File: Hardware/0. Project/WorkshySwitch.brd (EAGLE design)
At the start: 35 x 45 mm, 52 parts, among them J1 ICSP, K1 G3MB-202P, U2 HLK-PM01

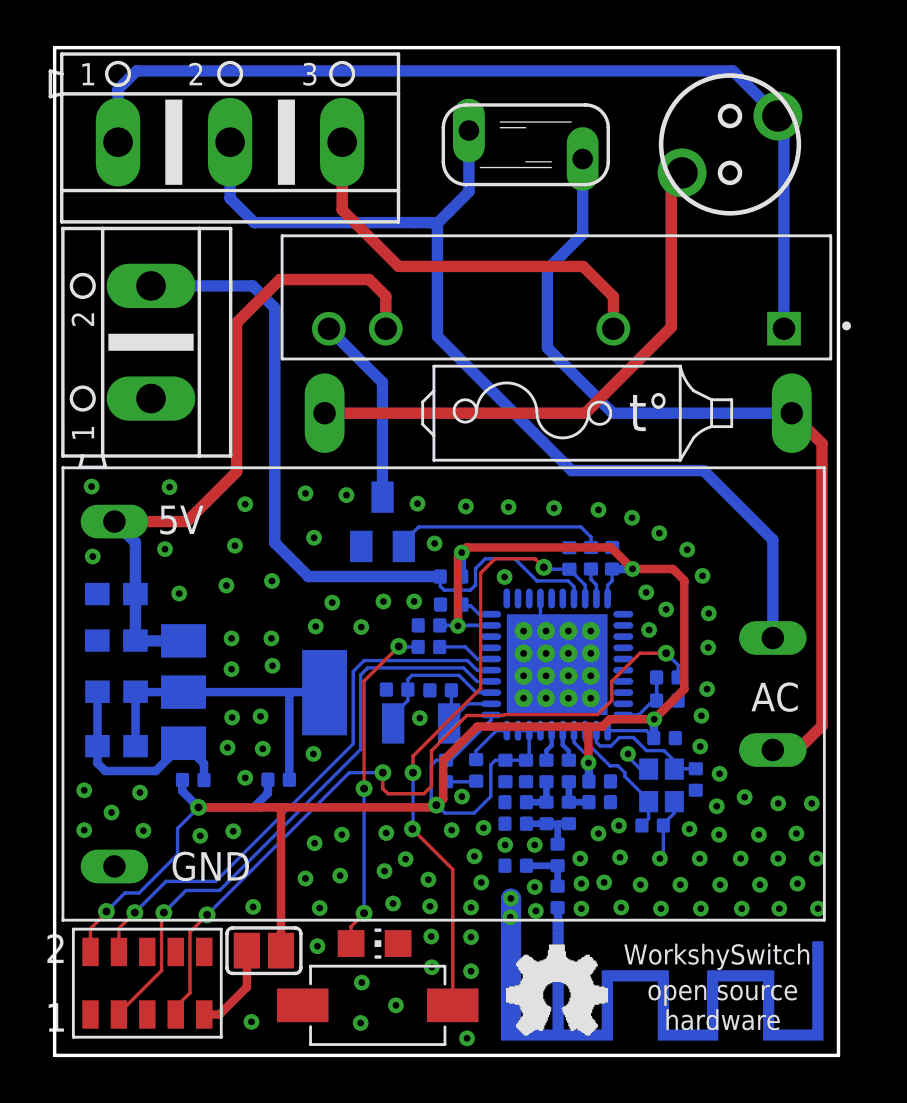
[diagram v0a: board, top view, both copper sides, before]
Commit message: 3D PCB Model Generated
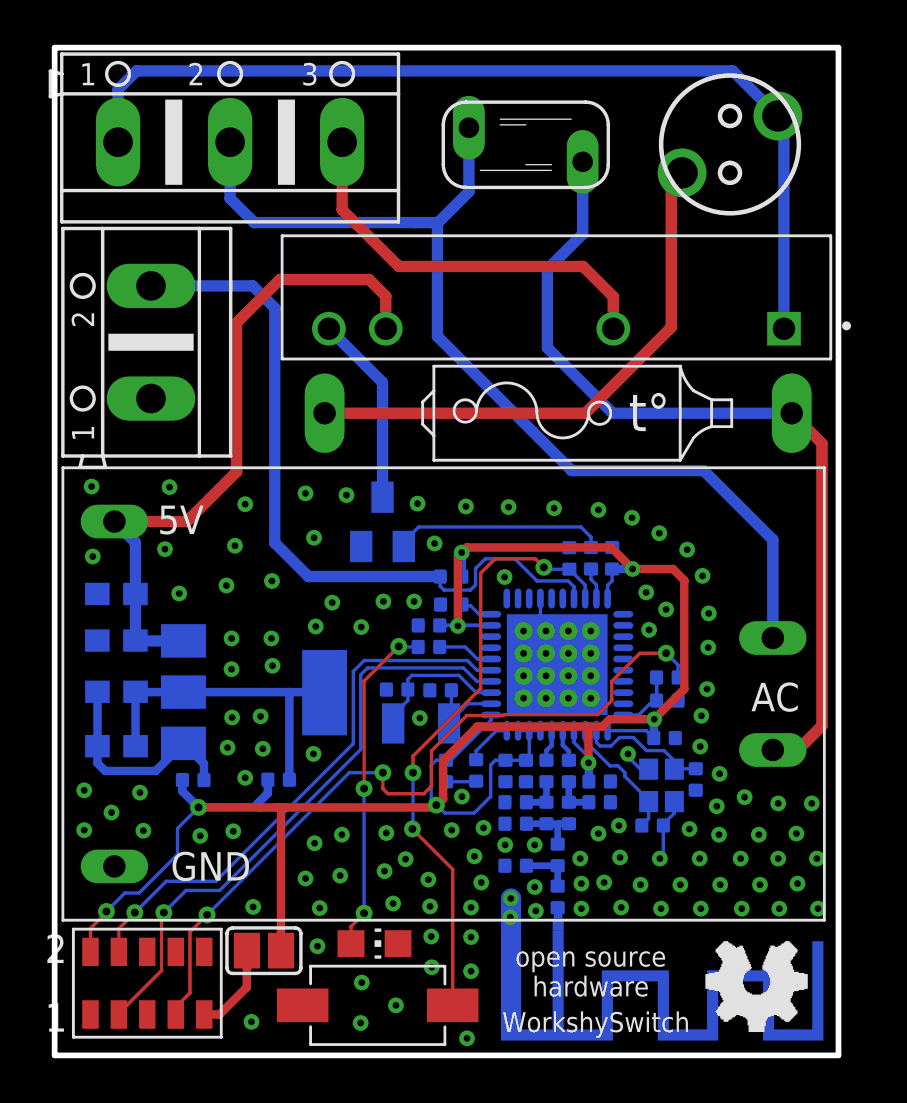
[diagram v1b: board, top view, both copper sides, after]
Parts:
- C22: value (none) -> C0402
- R5: device varistor:S05K11 -> varistor:S05K17

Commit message: Components values added
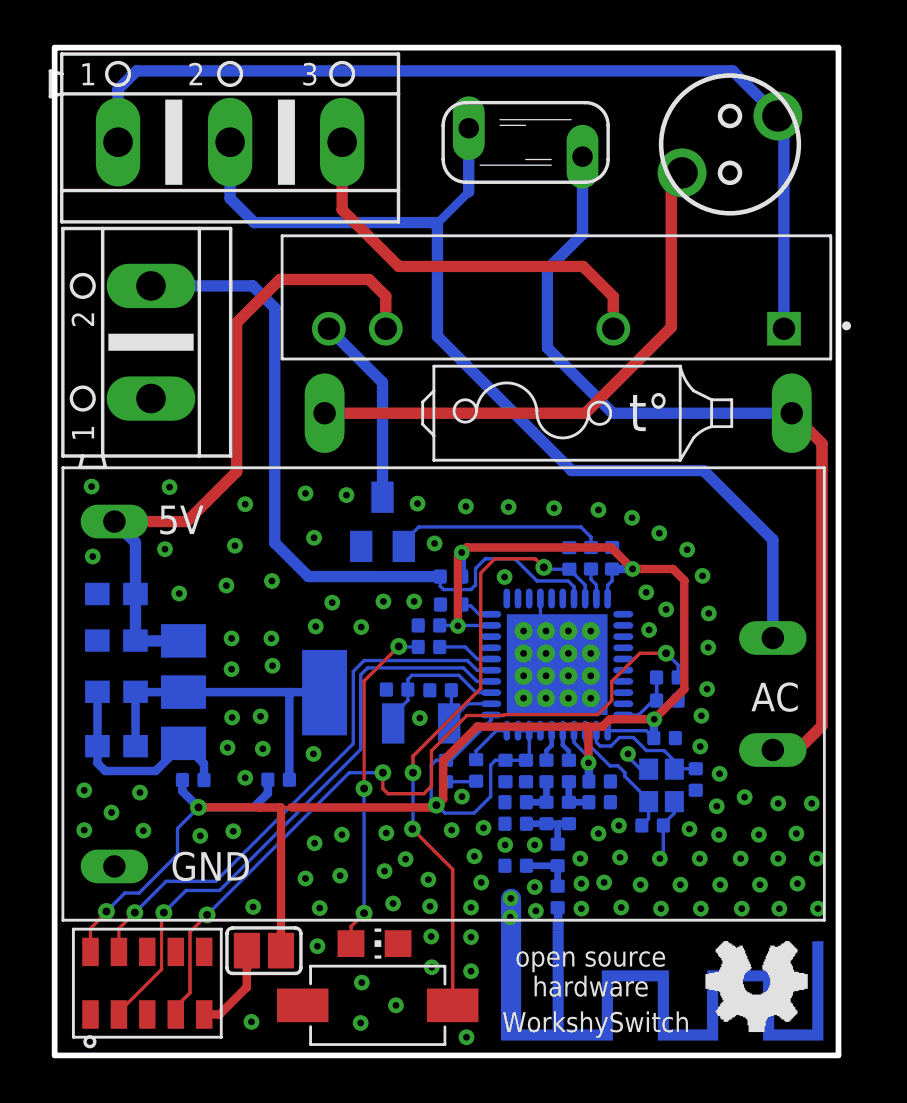
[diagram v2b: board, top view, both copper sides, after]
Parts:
- removed R5: 130VRMS, varistor:S05K17
- added R3: 130VRMS, varistor:S05K11
- C1, C26, C28, C29, C30, C31, C7: value (none) -> 100nF
- C18, C19: value (none) -> 18pF
- C2, C5: value (none) -> 10uF
- C21, C24: value (none) -> 1pF
- C22: value C0402 -> 1pF
- C25: value (none) -> 220pF
- C27, C32: value (none) -> 1uF
- C33, C34: value (none) -> 12pF
- C35, C36: value (none) -> 15pF
- C6: value (none) -> 2.2uF
- C9: value (none) -> 1nF
- L1, L2: value (none) -> 2nH
- L3: value (none) -> 1nH
- L4: value (none) -> 3nH
- L5: value (none) -> Ferrite Bead
- LED1: value (none) -> Green
- Q3: value (none) -> 32-MHz
- Q4: value (none) -> 32-kHz
- R1: value (none) -> 1k
- R10: value (none) -> 56k
- R2, R7: value (none) -> 10k
- R4: value (none) -> 4.7k
- R8: value (none) -> 2.7k
- SJ1: value (none) -> Jumper
- T1: value (none) -> BC848
- U1: value (none) -> LM1117-3.3
- U3: value (none) -> CC2541
- X1: value (none) -> Therminal Block 2 Vias
- X3: value (none) -> Therminal Bloc 3 Vias
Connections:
- net N$3: now also R3.2; no longer R5.2
- net N$4: now also R3.1; no longer R5.1
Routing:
- net 3.3V: track 100.4 -> 97.2 mm
- net N$3: track 46.6 -> 45.6 mm
